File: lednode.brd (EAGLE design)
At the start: 100 x 50 mm, 44 parts

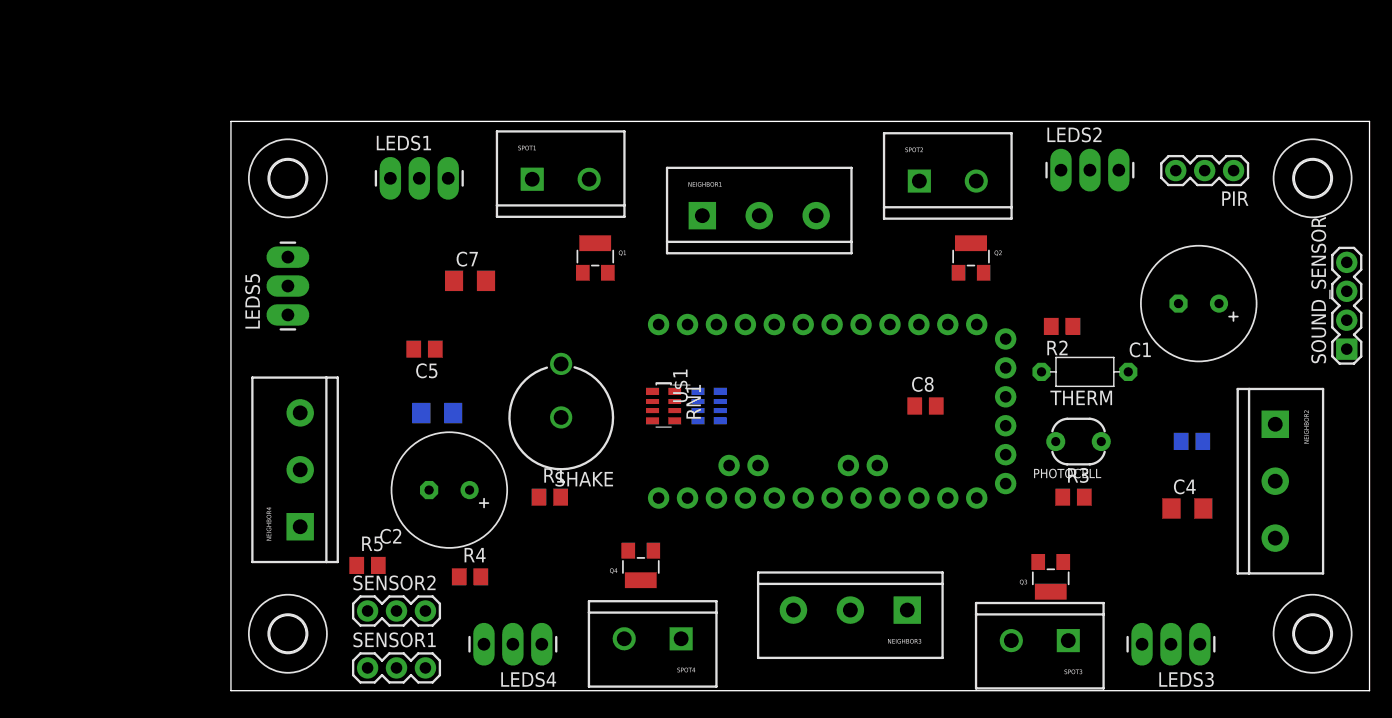
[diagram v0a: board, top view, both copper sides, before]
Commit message: Finetned lednode schema, laid out components on lednode board, started routing.
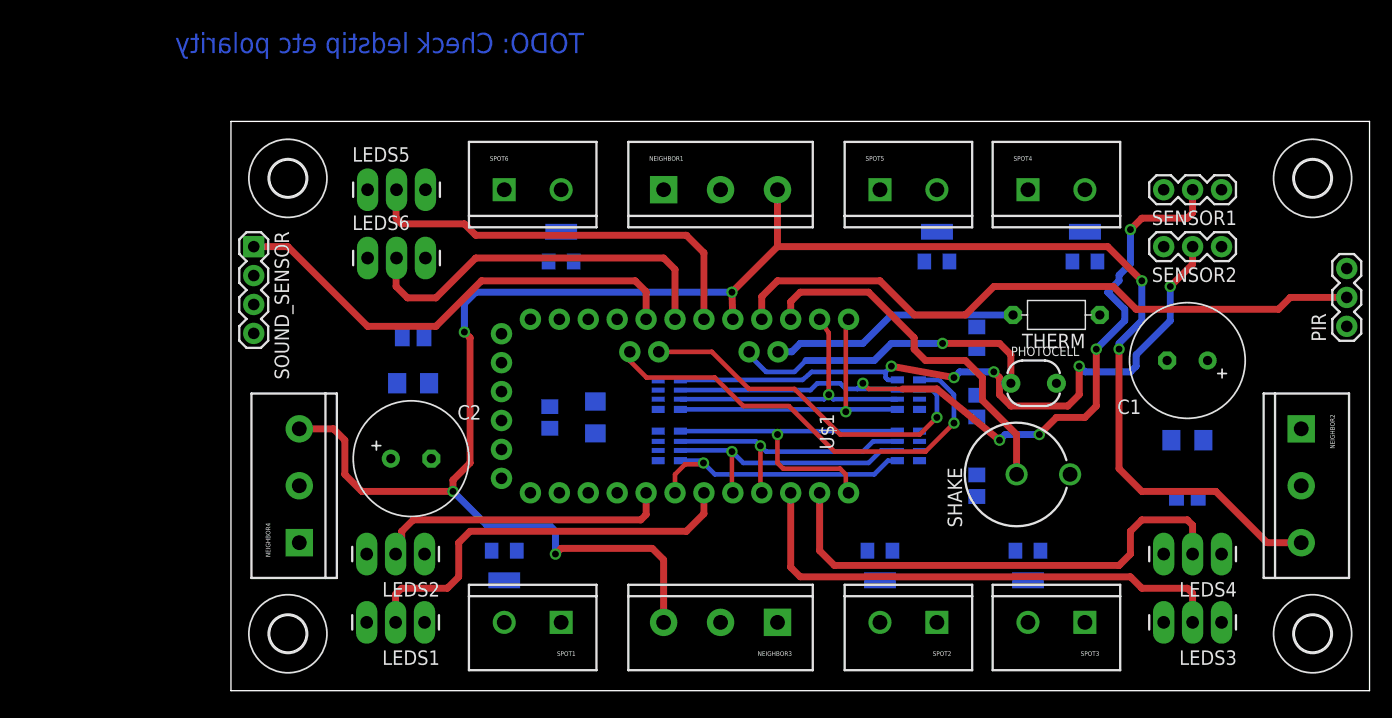
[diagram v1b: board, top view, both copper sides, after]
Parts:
- removed R4, R5: 10k, rcl:R0805
- added LEDS6: (no value), SparkFun-Connectors:1X03_LONGPADS
- added Q5, Q6: (no value), adafruit:SOT23-W
- added RN3: 220R, dp_devices:RN8P-4R-CRA06S
- added RN4: 10k, dp_devices:RN8P-4R-CRA06S
- added SPOT5, SPOT6: M025MM, SparkFun-Connectors:SCREWTERMINAL-5MM-2
- moved SOUND_SENSOR 96.4 mm to (2.00, 39.0), turned to 270 degrees
- moved SENSOR1 86.0 mm to (87.0, 44.0), turned to 180 degrees
- moved SENSOR2 81.5 mm to (87.0, 39.0), turned to 180 degrees
- moved LEDS2 65.3 mm to (17.0, 12.0), turned to 180 degrees
- moved LEDS4 60.2 mm to (87.0, 12.0)
- moved SPOT4 49.8 mm to (70.0, 44.0), turned to 0 degrees
- moved Q4 48.0 mm to (75.0, 39.0), flipped to the bottom, turned to 0 degrees
- moved SHAKE 40.3 mm to (69.0, 19.0), turned to 90 degrees
- moved LEDS1 39.1 mm to (17.0, 6.00), turned to 180 degrees
- moved SPOT1 39.0 mm to (29.0, 6.00), turned to 180 degrees
- moved SPOT2 38.8 mm to (62.0, 6.00), turned to 180 degrees
- moved R1 37.5 mm to (65.5, 18.0), flipped to the bottom, turned to 90 degrees
- moved C8 33.0 mm to (28.0, 24.0), flipped to the bottom, turned to 270 degrees
- moved Q1 28.2 mm to (24.0, 11.0), flipped to the bottom, turned to 180 degrees
- moved Q2 28.2 mm to (57.0, 11.0), flipped to the bottom, turned to 180 degrees
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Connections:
- removed net NEIGHBOR1: NEIGHBOR1.3, U$1.15
- removed net NEIGHBOR2: NEIGHBOR2.3, U$1.A5
- removed net NEIGHBOR3: NEIGHBOR3.3, U$1.A6
- removed net NEIGHBOR4: NEIGHBOR4.3, U$1.A7
- new net DATA_BUS: NEIGHBOR1.3, NEIGHBOR2.3, NEIGHBOR3.3, NEIGHBOR4.3, U$1.17
- new net LEDSTRIP6: LEDS6.2, U$1.19
- new net N$1: Q5.3, SPOT5.2
- new net N$11: Q6.3, SPOT6.2
- new net N$12: Q6.1, RN3.7
- new net N$8: Q5.1, RN3.8
- new net SENSOR1: RN3.3, RN4.6, SENSOR1.2
- new net SENSOR2: RN3.4, RN4.5, SENSOR2.2
- new net SPOTLIGHT5: RN3.1, RN4.8, U$1.13
- new net SPOTLIGHT6: RN3.2, RN4.7, U$1.14
- net +12V: now also LEDS6.1, SPOT5.1, SPOT6.1
- net EXTRA_SENSOR1: now also RN3.6, U$1.A4; no longer R4.2, SENSOR1.2, U$1.19
- net EXTRA_SENSOR2: now also RN3.5, U$1.A5; no longer R5.2, SENSOR2.2, U$1.20
- net GND: now also LEDS6.3, Q5.2, Q6.2, RN4.1, RN4.2, RN4.3, RN4.4; no longer R4.1, R5.1
- net LEDSTRIP1: now also U$1.7; no longer U$1.5
- net LEDSTRIP2: now also U$1.5; no longer U$1.6
- net LEDSTRIP3: now also U$1.10; no longer U$1.8
- net LEDSTRIP5: now also U$1.18; no longer U$1.10
- net LIGHTLEVEL: now also U$1.A7; no longer U$1.17
- net PROXIMITY: now also U$1.16; no longer U$1.7
- net SHAKE: now also U$1.15; no longer U$1.16
- net SOUND_ANALOG: now also U$1.20; no longer U$1.A4
- net SPOTLIGHT1: now also U$1.6; no longer U$1.9
- net SPOTLIGHT2: now also U$1.8; no longer U$1.12
- net SPOTLIGHT3: now also U$1.9; no longer U$1.13
- net SPOTLIGHT4: now also U$1.12; no longer U$1.14
- net TEMPERATURE: now also U$1.A6; no longer U$1.18
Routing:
- net DATA_BUS: track 0.00 -> 169.2 mm, vias 0 -> 6
- net SENSOR1: track 0.00 -> 69.9 mm, vias 0 -> 5
- net SENSOR2: track 0.00 -> 60.4 mm, vias 0 -> 5
- net PROXIMITY: track 0.00 -> 57.5 mm
- net LEDSTRIP3: track 0.00 -> 45.3 mm
- net LEDSTRIP4: track 0.00 -> 43.9 mm
- net SOUND_ANALOG: track 0.00 -> 41.8 mm
- net EXTRA_SENSOR2: track 0.00 -> 39.7 mm, vias 0 -> 1
- net LEDSTRIP5: track 0.00 -> 36.7 mm
- net LEDSTRIP1: track 0.00 -> 36.1 mm
- net LEDSTRIP6: track 0.00 -> 33.7 mm
- net SHAKE: track 0.00 -> 32.2 mm
- net EXTRA_SENSOR1: track 0.00 -> 31.7 mm, vias 0 -> 1
- net SPOTLIGHT4: track 0.00 -> 29.9 mm, vias 0 -> 1
- net LIGHTLEVEL: track 0.00 -> 27.8 mm, vias 0 -> 1
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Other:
- board text added: "TODO: Check ledstip etc polarity"

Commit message: Layout and routing done, silkscreens mostly done.
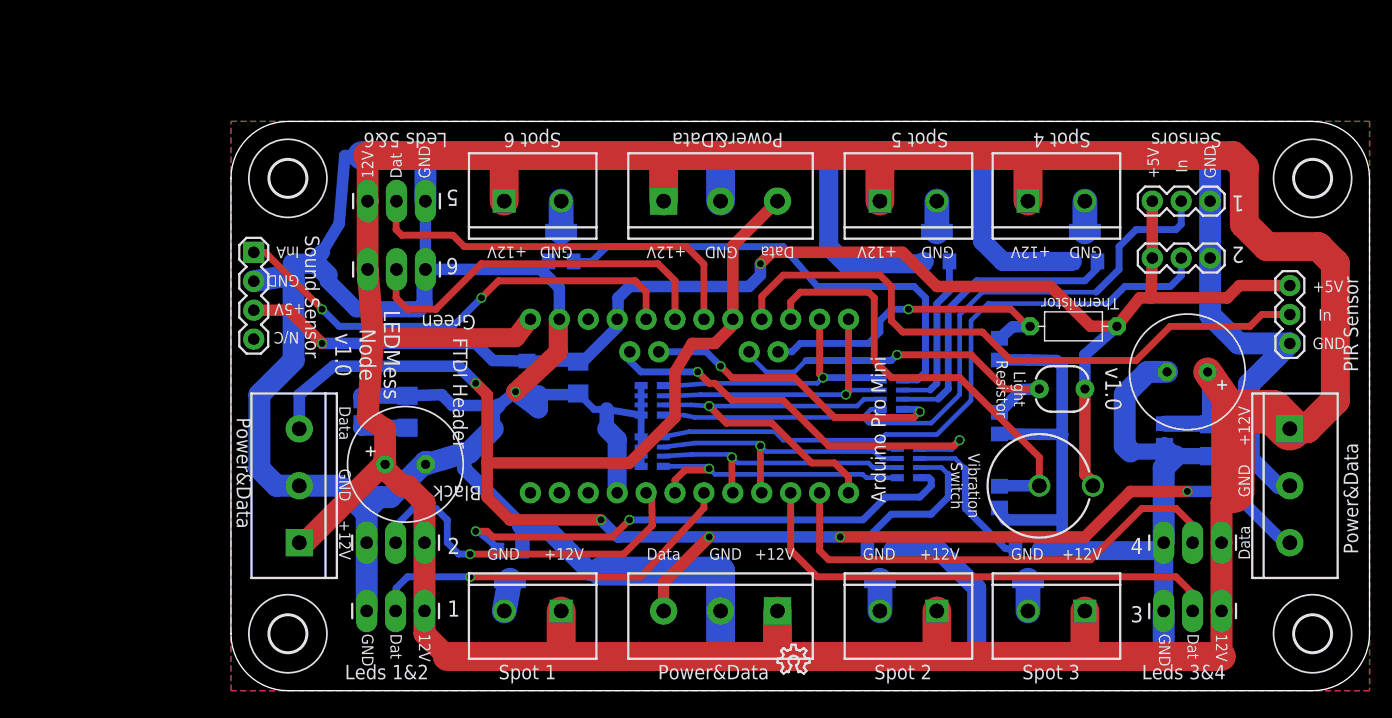
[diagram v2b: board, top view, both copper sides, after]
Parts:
- added LOGO3: LOGO-OSHW-8MILX0100-NT, Logo:OSHW_8X100_NOTEXT
- U$1: device SparkFun-Boards:ARDUINO_PRO_MINI -> SparkFun-Boards-with-arduino-pro-mini-without-connection-pins:ARDUINO_PRO_MINI
- moved C5 7.91 mm to (11.5, 24.5), turned to 90 degrees
- moved C6 5.85 mm to (82.0, 22.5), turned to 270 degrees
- moved PIR 5.22 mm to (93.0, 30.5)
- moved C8 4.47 mm to (26.0, 28.0)
- moved C7 3.81 mm to (30.5, 27.5)
- moved C3 2.55 mm to (15.5, 24.5), turned to 90 degrees
- moved PHOTOCELL 2.55 mm to (73.0, 26.5)
- moved R3 2.50 mm to (67.5, 23.5)
- moved R1 2.24 mm to (67.5, 17.0)
- moved R2 2.24 mm to (67.5, 30.0)
- moved SHAKE 2.24 mm to (71.0, 18.0)
- moved C4 2.00 mm to (86.0, 22.0), turned to 270 degrees
- moved THERM 1.80 mm to (74.0, 32.0)
- moved RN2 1.58 mm to (37.0, 21.0)
- moved RN4 1.58 mm to (37.0, 25.5)
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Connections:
- removed net SENSOR2: RN3.4, RN4.5, SENSOR2.2
- new net N$13: RN1.4, RN2.5, SENSOR2.2
- net EXTRA_SENSOR1: now also RN3.8; no longer RN3.6
- net EXTRA_SENSOR2: now also RN1.5; no longer RN3.5
- net N$10: now also Q5.1, RN3.6; no longer Q4.1, RN1.5
- net N$12: now also RN3.5; no longer RN3.7
- net N$8: now also Q4.1, RN3.7; no longer Q5.1, RN3.8
- net SENSOR1: now also RN3.1, RN4.8; no longer RN3.3, RN4.6
- net SPOTLIGHT4: now also RN3.2, RN4.7; no longer RN1.4, RN2.5
- net SPOTLIGHT5: now also RN3.3, RN4.6; no longer RN3.1, RN4.8
- net SPOTLIGHT6: now also RN3.4, RN4.5; no longer RN3.2, RN4.7
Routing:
- net GND: track 0.00 -> 491.0 mm, vias 0 -> 1
- net +12V: track 0.00 -> 333.4 mm
- net +5V: track 0.00 -> 127.3 mm, vias 0 -> 2
- net SENSOR2: track 60.4 -> 0.00 mm, vias 5 -> 0
- net N$13: track 0.00 -> 59.3 mm
- net N$6: track 0.00 -> 46.4 mm, vias 0 -> 2
- net N$12: track 0.00 -> 42.3 mm
- net N$8: track 0.00 -> 26.6 mm
- net N$7: track 0.00 -> 14.5 mm
- net N$10: track 0.00 -> 14.4 mm
- net N$9: track 0.00 -> 13.8 mm
- net DATA_BUS: track 169.2 -> 155.9 mm, vias 6 -> 5
- net SENSOR1: track 69.9 -> 62.1 mm, vias 5 -> 0
- net SHAKE: track 32.2 -> 39.0 mm
- net TEMPERATURE: track 22.0 -> 27.9 mm, vias 0 -> 1
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- added copper zone on layer 1, net +12V
- added copper zone on layer 16, net GND
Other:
- outline, holes or cut-outs redrawn
- board text added: "+12V"
- board text added: "+5V"
- board text added: "1"
- board text added: "12V"
- board text added: "2"
- board text added: "3"
- board text added: "4"
- board text added: "5"
- board text added: "6"
- board text added: "Arduino Pro Mini"
- board text added: "Black"
- board text added: "Dat"
- board text added: "Data"
- board text added: "FTDI Header"
- board text added: "GND"
- board text added: "Green"
- board text added: "In"
- board text added: "InA"
- board text added: "LDR Volt Div"
- board text added: "LEDMess Node v1.0"
- board text added: "Leds 1&2"
- board text added: "Leds 3&4"
- board text added: "Leds 5&6"
- board text added: "Light Resistor"
- board text added: "N/C"
- board text added: "PIR Sensor"
- board text added: "Power&Data"
- board text added: "Sensors"
- board text added: "Sound Sensor"
- board text added: "Spot 1"
- board text added: "Spot 2"
- board text added: "Spot 3"
- board text added: "Spot 4"
- board text added: "Spot 5"
- board text added: "Spot 6"
- board text added: "Therm Volt Div"
- board text added: "Thermistor"
- board text added: "Vibration Pulldown"
- board text added: "Vibration Switch"
- board text added: "github.com/zzorn/ledmess"
- board text added: "v1.0"

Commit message: Final touches.
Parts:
- removed H1, H2, H3, H4: MOUNT-HOLE3.2, holes:3,2
- added GND, RESET, RXI, TXO: (no value), SparkFun-Connectors:1X01NS-KIT
- PHOTOCELL: device SparkFun:PHOTOCELL -> SparkFun-Sensors:PHOTOCELL
- SOUND_SENSOR: device SparkFun-Connectors:1X04 -> SparkFun-Connectors:1X04_NO_SILK
- THERM: device discrete:R-7,5 -> discrete-fixed-thermistor-silk:R-7,5
- moved C8 4.00 mm to (30.0, 28.0), turned to 0 degrees
- moved C7 2.55 mm to (30.0, 25.0), turned to 0 degrees
- moved C2 0.20 mm to (15.3, 20.1)
- moved C3 0.20 mm to (15.5, 24.7)
- moved C5 0.20 mm to (11.5, 24.7)
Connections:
- new net N$14: TXO.1, U$1.1
- new net N$15: RXI.1, U$1.2
- new net N$16: RESET.1, U$1.3
- net GND: now also GND.1
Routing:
- net +5V: track 127.3 -> 135.6 mm, vias 2 -> 3
- net GND: track 491.0 -> 486.4 mm, vias 1 -> 0
- net DATA_BUS: track 155.9 -> 152.4 mm
- net LEDSTRIP6: track 35.0 -> 31.5 mm
- net +12V: track 333.4 -> 336.6 mm
- net N$16: track 0.00 -> 3.06 mm
- net N$15: track 0.00 -> 3.06 mm
- net N$14: track 0.00 -> 3.06 mm
- net N$12: track 42.3 -> 41.2 mm
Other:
- board text added: "RST"
- board text added: "RXI"
- board text added: "TXO"
- board text removed: "TODO: Check ledstip etc polarity"
- board text removed: "TODO: Remember sufficient hole size for screw terminals"

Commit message: Final cleanup and gerber generation.
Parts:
- GND, RESET, RXI, TXO: value (none) -> M01SMDNS; device SparkFun-Connectors:1X01NS-KIT -> SparkFun-Connectors:1X01NS
- Q1, Q2, Q3, Q4, Q5, Q6: value (none) -> AO3402
- moved LOGO3 2.50 mm to (50.5, 1.50), flipped to the bottom
- moved C7 1.00 mm to (30.0, 26.0)
- moved C8 1.00 mm to (30.0, 29.0)
- moved C3 0.50 mm to (15.0, 24.7)
- moved Q3 0.50 mm to (69.5, 11.0)
- moved Q5 0.50 mm to (62.5, 39.0)
- moved Q6 0.50 mm to (29.5, 39.0)
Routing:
- net GND: track 486.4 -> 497.2 mm
- net DATA_BUS: track 152.4 -> 146.1 mm, vias 5 -> 4
- net LEDSTRIP2: track 31.6 -> 27.9 mm
- net LEDSTRIP4: track 42.2 -> 38.6 mm
- net LEDSTRIP3: track 43.5 -> 42.0 mm
- net LEDSTRIP5: track 35.4 -> 33.9 mm
- net LEDSTRIP1: track 33.5 -> 32.4 mm
- net +5V: track 135.6 -> 136.6 mm
- net N$6: track 46.4 -> 47.4 mm
- net LEDSTRIP6: track 31.5 -> 30.7 mm
- net N$12: track 41.2 -> 40.5 mm
- net +12V: track 336.6 -> 336.0 mm
- net SHAKE: track 39.0 -> 38.4 mm
- net PROXIMITY: track 55.4 -> 54.9 mm
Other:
- board size 100 x 50 mm -> 99.8 x 49.8 mm
